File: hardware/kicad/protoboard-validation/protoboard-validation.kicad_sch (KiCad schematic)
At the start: 43 parts, among them J1 MONITOR_JOG, Q1 2N3904, Q2 2N3904, Q3 2N3904, Q4 2N3904, Q5 2N3904, Q6 2N3904, Q7 2N3904, Q8 S8550, Q9 2N3904, SW1 SW_Push, U1 ADS1115, U2 SN74AHCT125

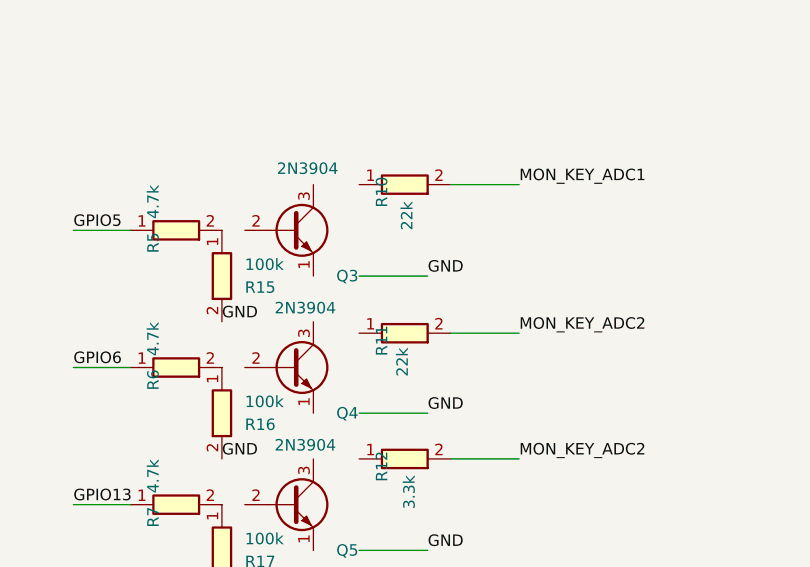
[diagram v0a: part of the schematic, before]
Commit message: Fix JOG up and center resistor values
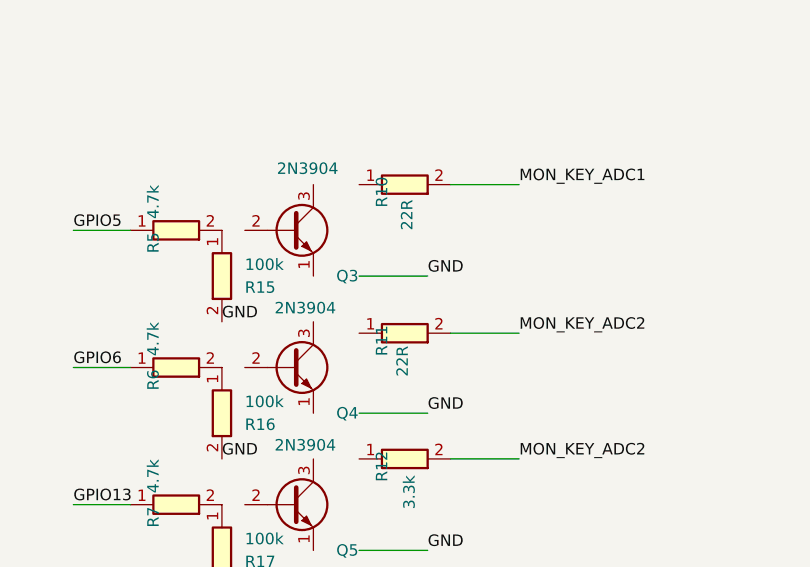
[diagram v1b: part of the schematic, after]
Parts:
- R10, R11: value 22k -> 22R
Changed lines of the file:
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@@
 			)
 		)
-		(property "Value" "22k"
+		(property "Value" "22R"
 			(at 146.304 99.06 0)
 			(show_name no)
@@
 			)
 		)
-		(property "Value" "22k"
+		(property "Value" "22R"
 			(at 145.796 115.316 0)
 			(show_name no)
